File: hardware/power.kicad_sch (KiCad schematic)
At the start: 36 parts, among them Q4 DMN1150UFB-7B, U3 TI LMR51430YFDDCR, U4 TI LMR51430YFDDCR, U5 TPS2116DRLR, U6 NCV8187AMT180TAG, U7 LP5912-3.3DRVR

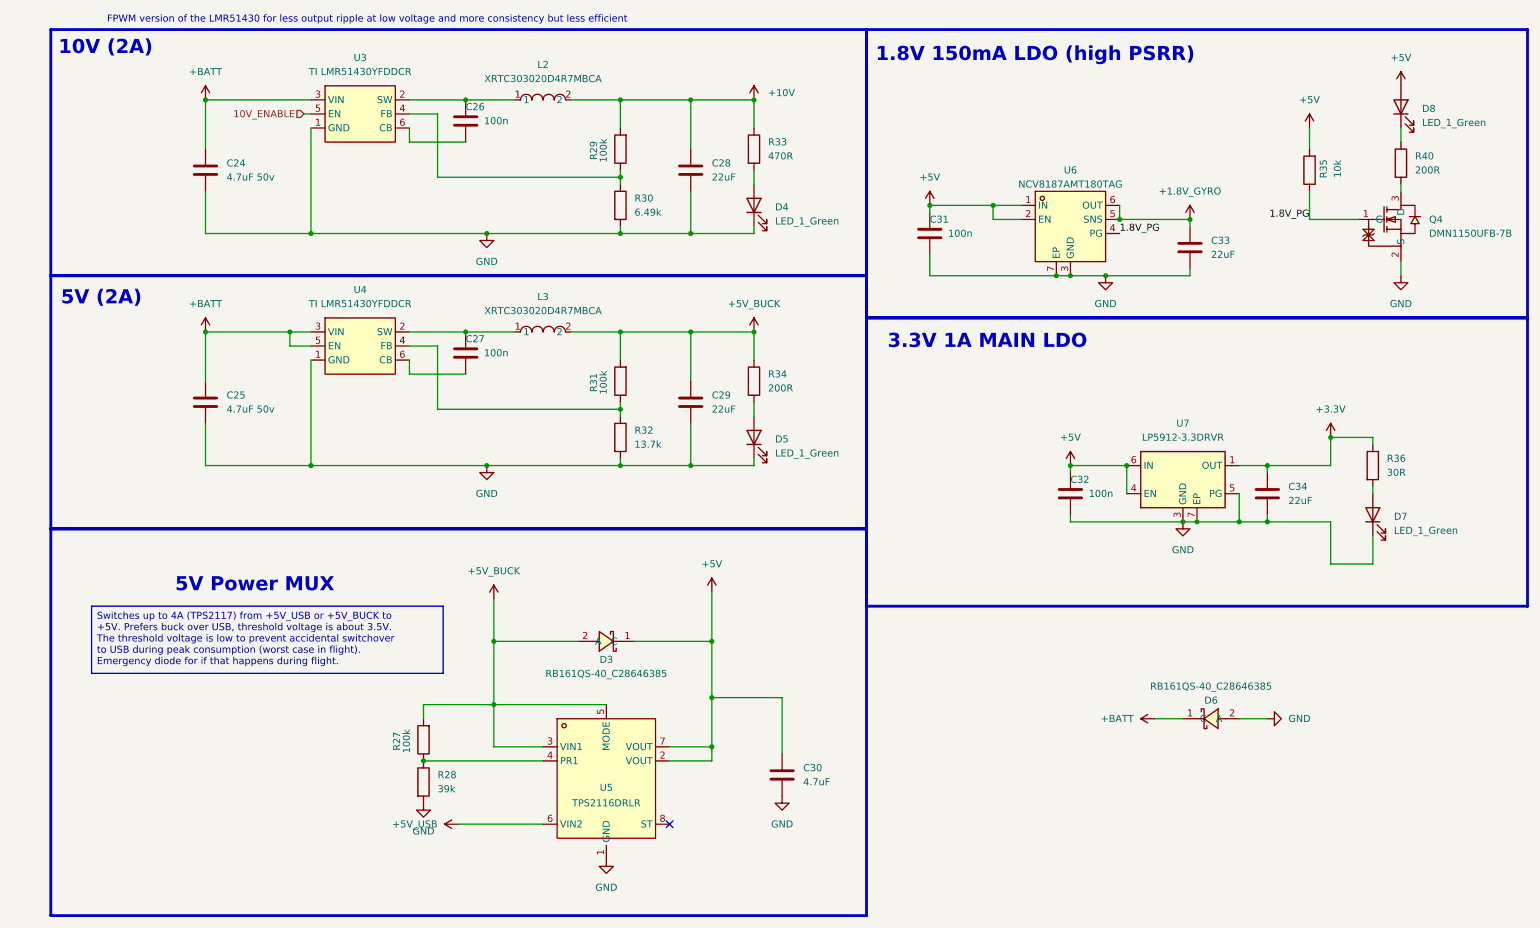
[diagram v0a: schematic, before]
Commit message: some minor tweaks
- remove some unnecessary resistors
- slightly higher 10V rail to account for voltage drop
- some cleanup
- simpler PG 1.8V circuit
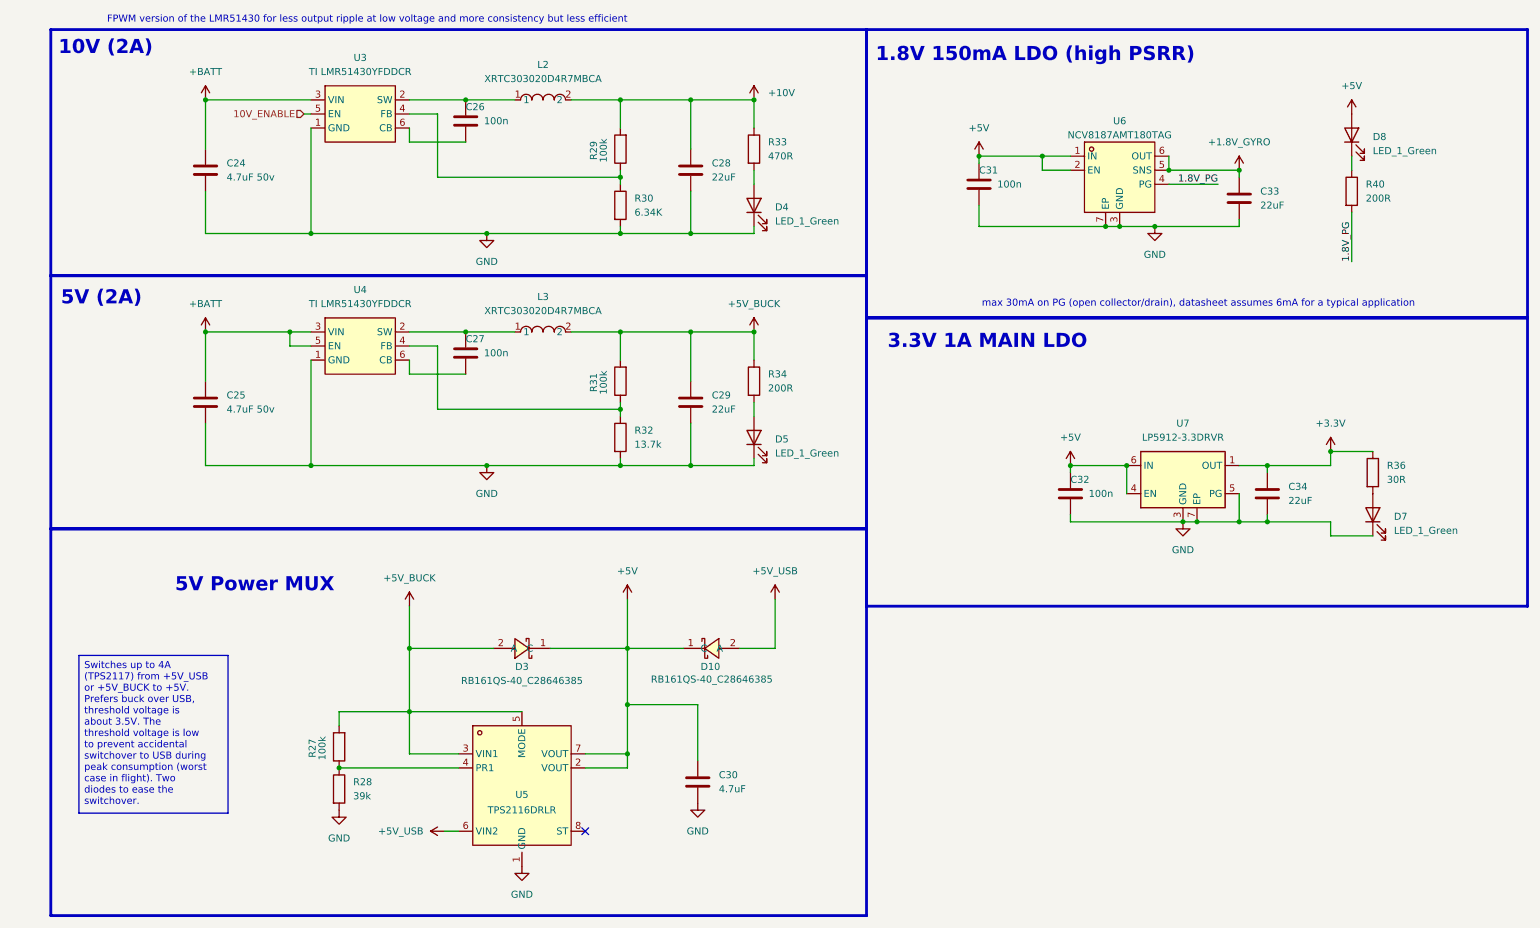
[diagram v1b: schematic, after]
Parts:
- removed D6: RB161QS-40_C28646385, lib:SOD-882_L1.0-W0.6-RD, symbol lib:RB161QS-40_C28646385
- removed Q4: DMN1150UFB-7B, lib:DFN-3L_L1.0-W0.6-P0.65-BR, symbol lib:DMN1150UFB-7B
- removed R35: 10k, Resistor_SMD:R_0201_0603Metric, symbol Device:R
- added D10: RB161QS-40_C28646385, lib:SOD-882_L1.0-W0.6-RD, symbol lib:RB161QS-40_C28646385
- R30: value 6.49k -> 6.34K; LCSC C474786 -> C100502; MPN RC0201FR-076K8L -> (none); Manufacturer YAGEO -> LIZ Elec
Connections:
- net +5V: now also D10.1 (C)
- net +5V_USB: now also D10.2 (A)
- net 1.8V_PG: now also R40.2
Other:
- note added: "max 30mA on PG (open collector/drain), datasheet assumes 6mA for a typical application"
- moved on the sheet: C30, C31, C33, D3, D8, R27, R28, R36, R40, U5, U6
